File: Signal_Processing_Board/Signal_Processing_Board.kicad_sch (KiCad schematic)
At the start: 18 parts, among them J1 Screw_Terminal_01x02, J10 Conn_01x01_Socket, J11 Conn_01x01_Socket, J2 Screw_Terminal_01x03, J3 Screw_Terminal_01x02, J6 Conn_01x01_Socket, J7 Conn_01x01_Socket, J8 Conn_01x01_Socket, J9 Conn_01x01_Socket

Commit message: Roughly Finalized Signal processing board
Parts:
- added H1, H2, H3, H4: MountingHole, MountingHole:MountingHole_3.2mm_M3_ISO7380_Pad, symbol Mechanical:MountingHole_Pad
- added J12, J13, J14: Conn_01x01_Socket, TestPoint:TestPoint_THTPad_D1.5mm_Drill0.7mm, symbol Connector:Conn_01x01_Socket
- U7, U9: footprint Custom_parts:BreadBoard Space -> Custom_parts:BreadBoard Space XL
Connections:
- net +15V: now also J12.1 (Pin_1)
- net -15V: now also J14.1 (Pin_1)
- net GND: now also H1.1, H2.1, H3.1, H4.1, J13.1 (Pin_1)

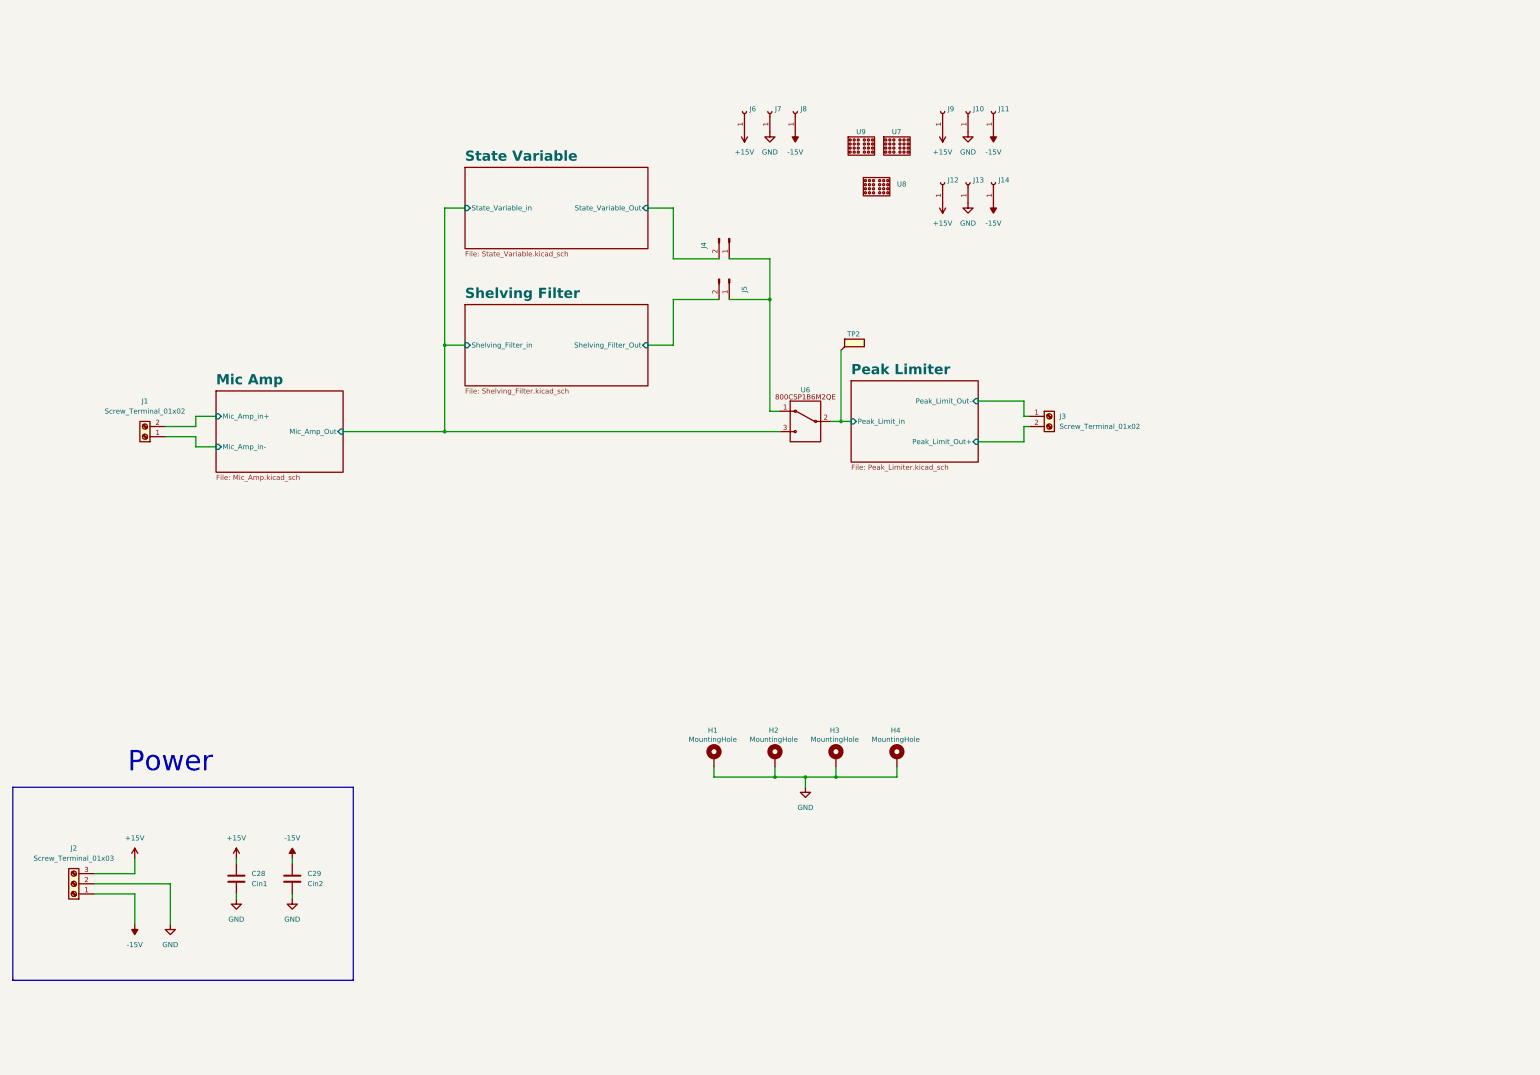
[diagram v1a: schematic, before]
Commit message: Updated Schematic and initial layout of combined board
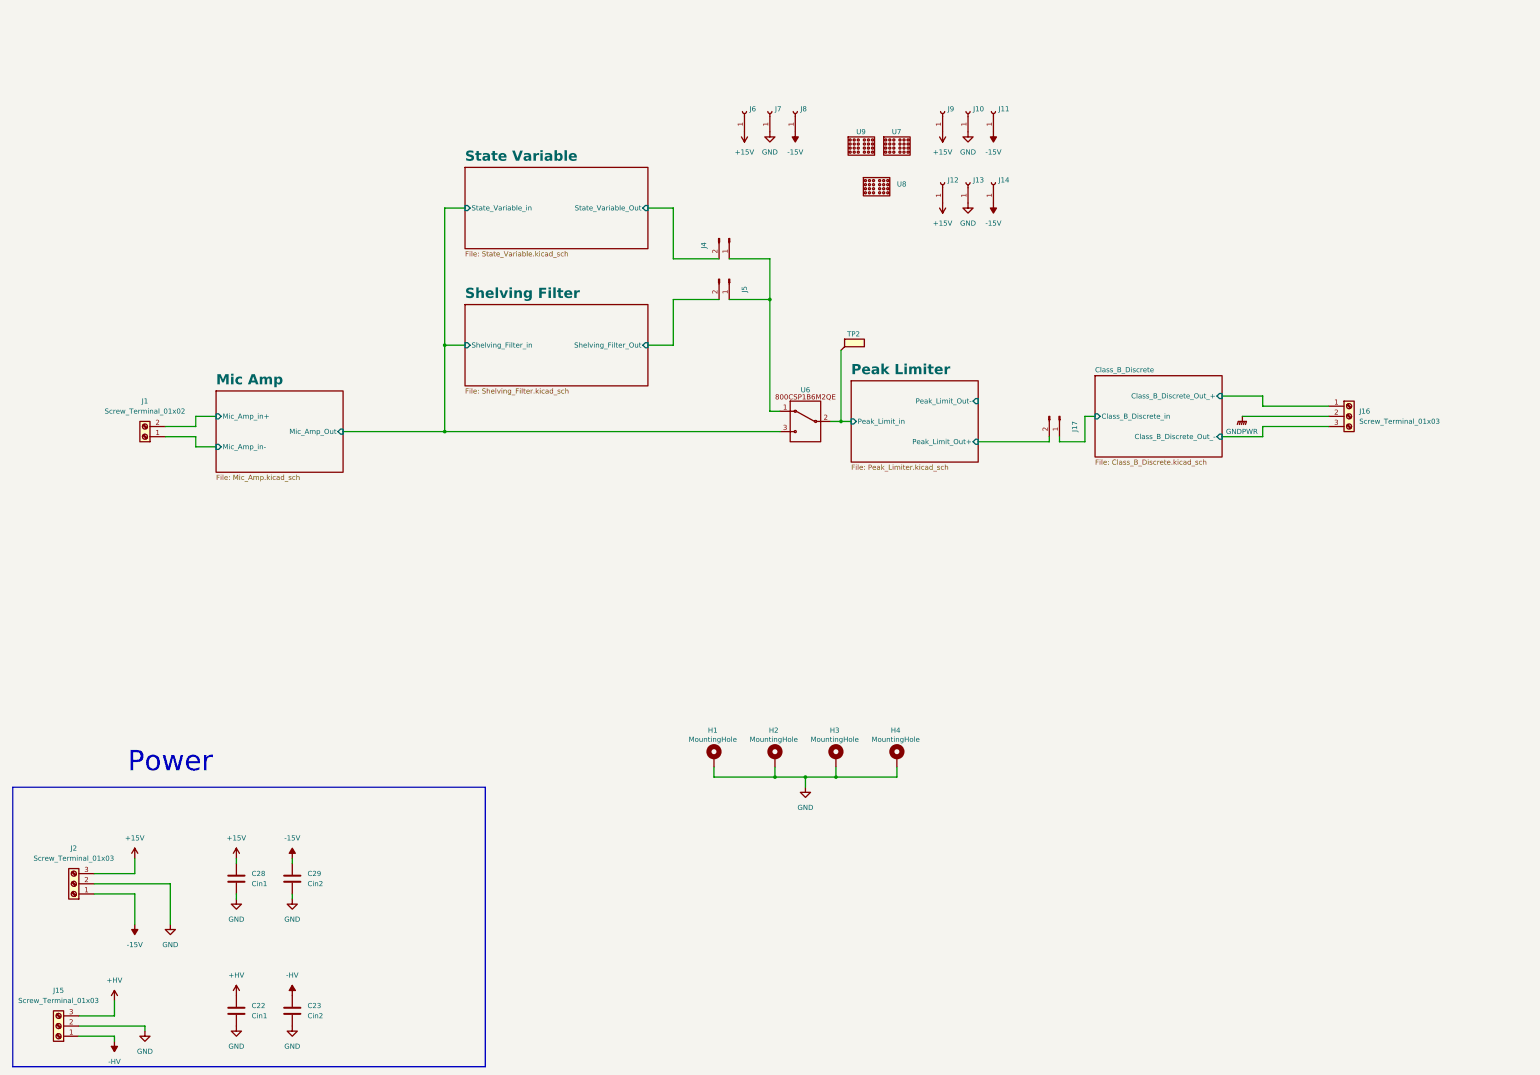
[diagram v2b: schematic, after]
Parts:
- removed J3: Screw_Terminal_01x02, TerminalBlock_TE-Connectivity:TerminalBlock_TE_282834-2_1x02_P2.54mm_Horizontal, symbol Connector:Screw_Terminal_01x02
- added C22: Cin1, Capacitor_THT:CP_Radial_D10.0mm_P5.00mm, symbol Device:C
- added C23: Cin2, Capacitor_THT:CP_Radial_D10.0mm_P5.00mm, symbol Device:C
- added J15, J16: Screw_Terminal_01x03, TerminalBlock_TE-Connectivity:TerminalBlock_TE_282834-3_1x03_P2.54mm_Horizontal, symbol Connector:Screw_Terminal_01x03
- added J17: ~, Connector_PinHeader_2.54mm:PinHeader_1x02_P2.54mm_Vertical, symbol Connector:Conn_01x02_Pin
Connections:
- net GND: now also C22.2, C23.2, J15.2 (Pin_2)
- net Peak Limiter/Peak_Limit_Out+: now also J17.2 (Pin_2)
- new net +HV: C22.1, J15.3 (Pin_3)
- new net -HV: C23.1, J15.1 (Pin_1)
- new net Class_B_Discrete/Class_B_Discrete_Out_+: J16.1 (Pin_1)
- new net Class_B_Discrete/Class_B_Discrete_Out_-: J16.3 (Pin_3)
- new net Class_B_Discrete/Class_B_Discrete_in: J17.1 (Pin_1)
- new net GNDPWR: J16.2 (Pin_2)
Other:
- added sheet Class_B_Discrete (Class_B_Discrete.kicad_sch)

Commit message: First semi-finalized layout done
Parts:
- added H5, H6, H7, H8: MountingHole, MountingHole:MountingHole_3.2mm_M3_ISO7380_Pad, symbol Mechanical:MountingHole_Pad
- added J18, J19, J3: Conn_01x01_Socket, TestPoint:TestPoint_THTPad_D1.5mm_Drill0.7mm, symbol Connector:Conn_01x01_Socket
- added U13: ~, Custom_parts:BreadBoard Space XL, symbol Custom_parts:BreadBoard_Space
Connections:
- net +HV: now also J3.1 (Pin_1)
- net -HV: now also J19.1 (Pin_1)
- net GND: now also H5.1, H6.1, H7.1, H8.1, J18.1 (Pin_1); no longer C22.2, C23.2, J15.2 (Pin_2)
- net GNDPWR: now also C22.2, C23.2, J15.2 (Pin_2)

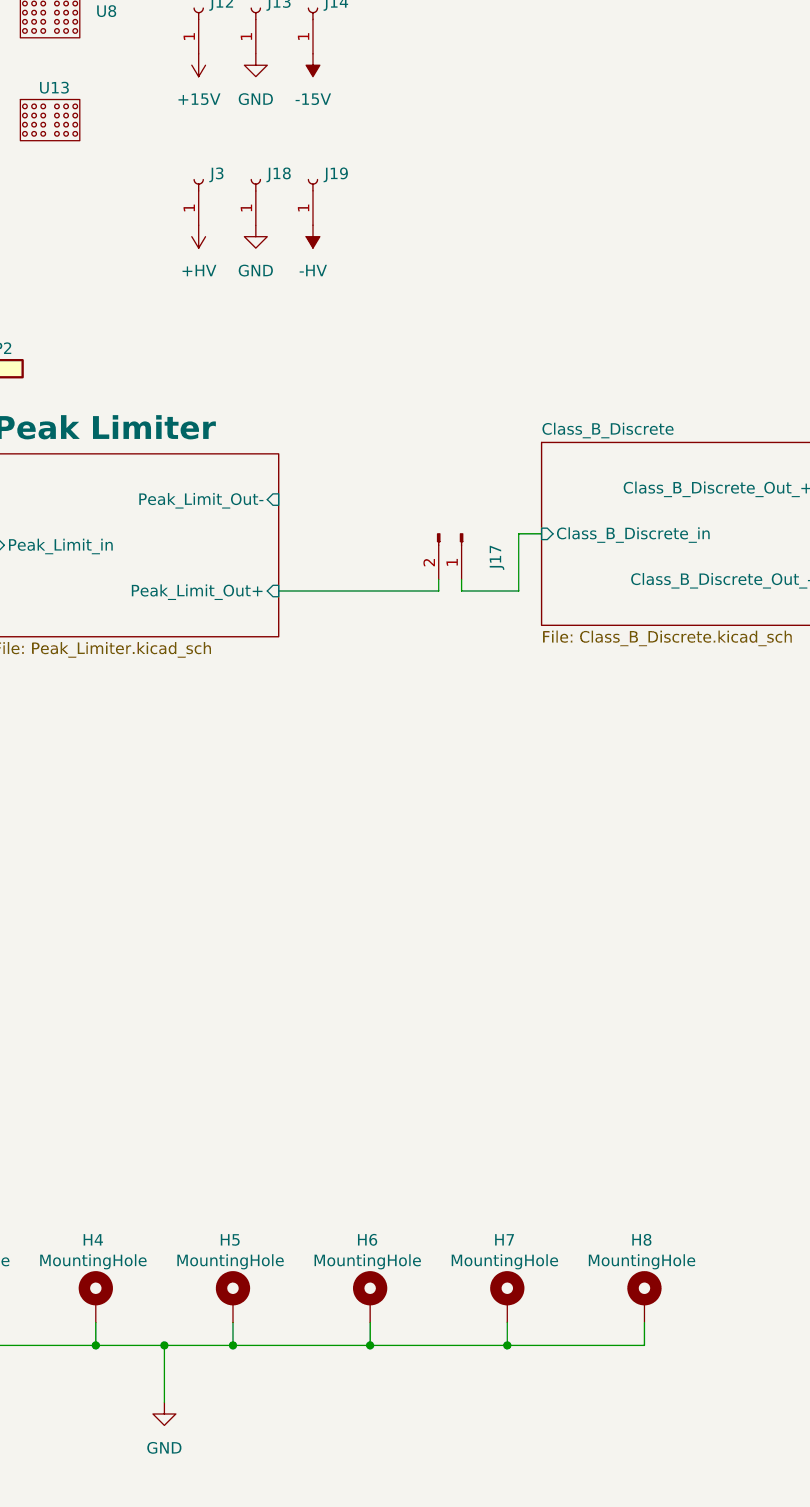
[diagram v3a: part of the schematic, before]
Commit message: First ordered version of Board
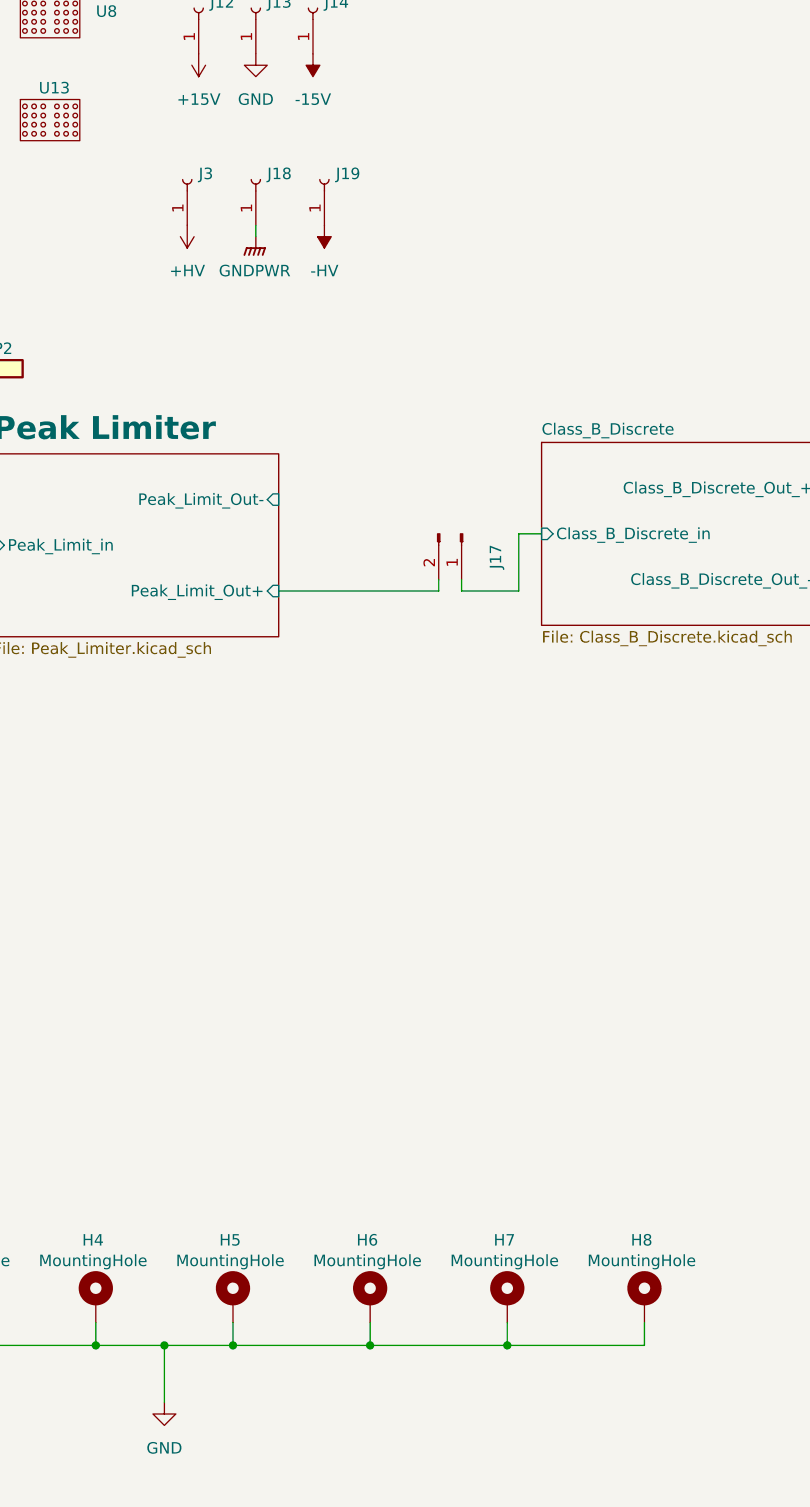
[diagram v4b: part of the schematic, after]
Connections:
- net GND: no longer J18.1 (Pin_1)
- net GNDPWR: now also J18.1 (Pin_1)
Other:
- moved on the sheet: J19, J3
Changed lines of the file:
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@@
 	(paper "A3")
 	(junction
-		(at 288.29 208.28)
-		(diameter 0)
-		(color 0 0 0 0)
-	)
-	(junction
 		(at 257.81 208.28)
 		(diameter 0)
@@
 	)
 	(junction
-		(at 212.09 208.28)
+		(at 288.29 208.28)
 		(diameter 0)
 		(color 0 0 0 0)
 	)
 	(junction
-		(at 273.05 208.28)
+		(at 212.09 208.28)
 		(diameter 0)
 		(color 0 0 0 0)
@@
 		(color 0 0 0 0)
 	)
+	(junction
+		(at 273.05 208.28)
+		(diameter 0)
+		(color 0 0 0 0)
+	)
 	(wire
 		(pts
@@
 	(wire
 		(pts
+			(xy 273.05 208.28) (xy 288.29 208.28)
+		)
+		(stroke
+			(width 0)
+			(type default)
+		)
+	)
+	(wire
+		(pts
 			(xy 334.01 113.03) (xy 323.85 113.03)
 		)
@@
 	(wire
 		(pts
-			(xy 288.29 208.28) (xy 273.05 208.28)
-		)
-		(stroke
-			(width 0)
-			(type default)
-		)
-	)
-	(wire
-		(pts
 			(xy 134.62 100.33) (xy 129.54 100.33)
 		)
@@
 	(wire
 		(pts
-			(xy 283.21 124.46) (xy 289.56 124.46)
+			(xy 260.35 85.09) (xy 260.35 83.82)
 		)
 		(stroke
@@
 	(wire
 		(pts
-			(xy 303.53 208.28) (xy 288.29 208.28)
+			(xy 283.21 124.46) (xy 289.56 124.46)
 		)
 		(stroke
@@
 	(wire
 		(pts
+			(xy 288.29 208.28) (xy 303.53 208.28)
+		)
+		(stroke
+			(width 0)
+			(type default)
+		)
+	)
+	(wire
+		(pts
 			(xy 250.19 208.28) (xy 250.19 214.63)
 		)
@@
 	(symbol
 		(lib_id "power:VCC")
-		(at 254 83.82 180)
+		(at 252.73 83.82 180)
 		(unit 1)
 		(exclude_from_sim no)
@@
 		(fields_autoplaced yes)
 		(property "Reference" "#PWR090"
-			(at 254 80.01 0)
+			(at 252.73 80.01 0)
 			(effects
 				(font
@@
 		)
 		(property "Value" "+HV"
-			(at 254 88.9 0)
+			(at 252.73 88.9 0)
 			(effects
 				(font
@@
 		)
 		(property "Footprint" ""
-			(at 254 83.82 0)
+			(at 252.73 83.82 0)
 			(effects
 				(font
@@
 		)
 		(property "Datasheet" ""
-			(at 254 83.82 0)
+			(at 252.73 83.82 0)
 			(effects
 				(font
@@
 		)
 		(property "Description" "Power symbol creates a global label with name \"VCC\""
-			(at 254 83.82 0)
+			(at 252.73 83.82 0)
 			(effects
 				(font
@@
 	)
 	(symbol
+		(lib_id "power:GNDPWR")
+		(at 260.35 85.09 0)
+		(unit 1)
+		(exclude_from_sim no)
+		(in_bom yes)
+		(on_board yes)
+		(dnp no)
+		(fields_autoplaced yes)
+		(property "Reference" "#PWR091"
+			(at 260.35 90.17 0)
+			(effects
+				(font
+					(size 1.27 1.27)
+				)
+				(hide yes)
+			)
+		)
+		(property "Value" "GNDPWR"
+			(at 260.223 88.9 0)
+			(effects
+				(font
+					(size 1.27 1.27)
+				)
+			)
+		)
+		(property "Footprint" ""
+			(at 260.35 86.36 0)
+			(effects
+				(font
+					(size 1.27 1.27)
+				)
+				(hide yes)
+			)
+		)
+		(property "Datasheet" ""
+			(at 260.35 86.36 0)
+			(effects
+				(font
+					(size 1.27 1.27)
+				)
+				(hide yes)
+			)
+		)
+		(property "Description" "Power symbol creates a global label with name \"GNDPWR\" , global ground"
+			(at 260.35 85.09 0)
+			(effects
+				(font
+					(size 1.27 1.27)
+				)
+				(hide yes)
+			)
+		)
+		(pin "1"
+		)
+		(instances
+			(project "Signal_Processing_Board"
+				(path "/f1e8215e-2100-40b3-b836-5691fd657e21"
+					(reference "#PWR091")
+					(unit 1)
+				)
+			)
+		)
+	)
+	(symbol
 		(lib_id "power:+15V")
 		(at 254 46.99 180)
@@
 	(symbol
 		(lib_id "Connector:Conn_01x01_Socket")
-		(at 254 78.74 90)
+		(at 252.73 78.74 90)
 		(unit 1)
 		(exclude_from_sim no)
@@
 		(fields_autoplaced yes)
 		(property "Reference" "J3"
-			(at 255.27 78.1049 90)
+			(at 254 78.1049 90)
 			(effects
 				(font
@@
 		)
 		(property "Value" "Conn_01x01_Socket"
-			(at 255.27 80.6449 90)
+			(at 254 80.6449 90)
 			(effects
 				(font
@@
 		)
 		(property "Footprint" "TestPoint:TestPoint_THTPad_D1.5mm_Drill0.7mm"
-			(at 254 78.74 0)
+			(at 252.73 78.74 0)
 			(effects
 				(font
@@
 		)
 		(property "Datasheet" "~"
-			(at 254 78.74 0)
+			(at 252.73 78.74 0)
 			(effects
 				(font
@@
 		)
 		(property "Description" "Generic connector, single row, 01x01, script generated"
-			(at 254 78.74 0)
+			(at 252.73 78.74 0)
 			(effects
 				(font
@@
 	)
 	(symbol
-		(lib_id "power:GND")
-		(at 260.35 83.82 0)
-		(unit 1)
-		(exclude_from_sim no)
-		(in_bom yes)
-		(on_board yes)
-		(dnp no)
-		(fields_autoplaced yes)
-		(property "Reference" "#PWR091"
-			(at 260.35 90.17 0)
-			(effects
-				(font
-					(size 1.27 1.27)
-				)
-				(hide yes)
-			)
-		)
-		(property "Value" "GND"
-			(at 260.35 88.9 0)
-			(effects
-				(font
-					(size 1.27 1.27)
-				)
-			)
-		)
-		(property "Footprint" ""
-			(at 260.35 83.82 0)
-			(effects
-				(font
-					(size 1.27 1.27)
-				)
-				(hide yes)
-			)
-		)
-		(property "Datasheet" ""
-			(at 260.35 83.82 0)
-			(effects
-				(font
-					(size 1.27 1.27)
-				)
-				(hide yes)
-			)
-		)
-		(property "Description" "Power symbol creates a global label with name \"GND\" , ground"
-			(at 260.35 83.82 0)
-			(effects
-				(font
-					(size 1.27 1.27)
-				)
-				(hide yes)
-			)
-		)
-		(pin "1"
-		)
-		(instances
-			(project "Signal_Processing_Board"
-				(path "/f1e8215e-2100-40b3-b836-5691fd657e21"
-					(reference "#PWR091")
-					(unit 1)
-				)
-			)
-		)
-	)
-	(symbol
 		(lib_id "Custom_parts:BreadBoard_Space")
 		(at 242.57 50.8 0)
@@
 	(symbol
 		(lib_id "power:VSS")
-		(at 266.7 83.82 180)
+		(at 267.97 83.82 180)
 		(unit 1)
 		(exclude_from_sim no)
@@
 		(fields_autoplaced yes)
 		(property "Reference" "#PWR092"
-			(at 266.7 80.01 0)
+			(at 267.97 80.01 0)
 			(effects
 				(font
@@
 		)
 		(property "Value" "-HV"
-			(at 266.7 88.9 0)
+			(at 267.97 88.9 0)
 			(effects
 				(font
@@
 		)
 		(property "Footprint" ""
-			(at 266.7 83.82 0)
+			(at 267.97 83.82 0)
 			(effects
 				(font
@@
 		)
 		(property "Datasheet" ""
-			(at 266.7 83.82 0)
+			(at 267.97 83.82 0)
 			(effects
 				(font
@@
 		)
 		(property "Description" "Power symbol creates a global label with name \"VSS\""
-			(at 266.7 83.82 0)
+			(at 267.97 83.82 0)
 			(effects
 				(font
@@
 	(symbol
 		(lib_id "Connector:Conn_01x01_Socket")
-		(at 266.7 78.74 90)
+		(at 267.97 78.74 90)
 		(unit 1)
 		(exclude_from_sim no)
@@
 		(fields_autoplaced yes)
 		(property "Reference" "J19"
-			(at 267.97 78.1049 90)
+			(at 269.24 78.1049 90)
 			(effects
 				(font
@@
 		)
 		(property "Value" "Conn_01x01_Socket"
-			(at 267.97 80.6449 90)
+			(at 269.24 80.6449 90)
 			(effects
 				(font
@@
 		)
 		(property "Footprint" "TestPoint:TestPoint_THTPad_D1.5mm_Drill0.7mm"
-			(at 266.7 78.74 0)
+			(at 267.97 78.74 0)
 			(effects
 				(font
@@
 		)
 		(property "Datasheet" "~"
-			(at 266.7 78.74 0)
+			(at 267.97 78.74 0)
 			(effects
 				(font
@@
 		)
 		(property "Description" "Generic connector, single row, 01x01, script generated"
-			(at 266.7 78.74 0)
+			(at 267.97 78.74 0)
 			(effects
 				(font
